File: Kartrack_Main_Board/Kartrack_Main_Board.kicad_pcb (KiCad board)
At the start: 4 copper layers, 130 x 80 mm, 69 parts, among them IC1 MIC3172YM, J2 Conn_Coaxial, J3 Conn_Coaxial, J4 Conn_01x02_Socket, J5 Conn_01x02_Socket, J6 USB_C_Receptacle_PowerOnly_6P, Q1 RE1C, SW1 SW_Push, SW2 SW_Push, SW3 SW_Push, U2 L76L-M33, U3 Ai-Thinker-Ra-02, U4 BQ21040DBV, U5 BU33SD5WG

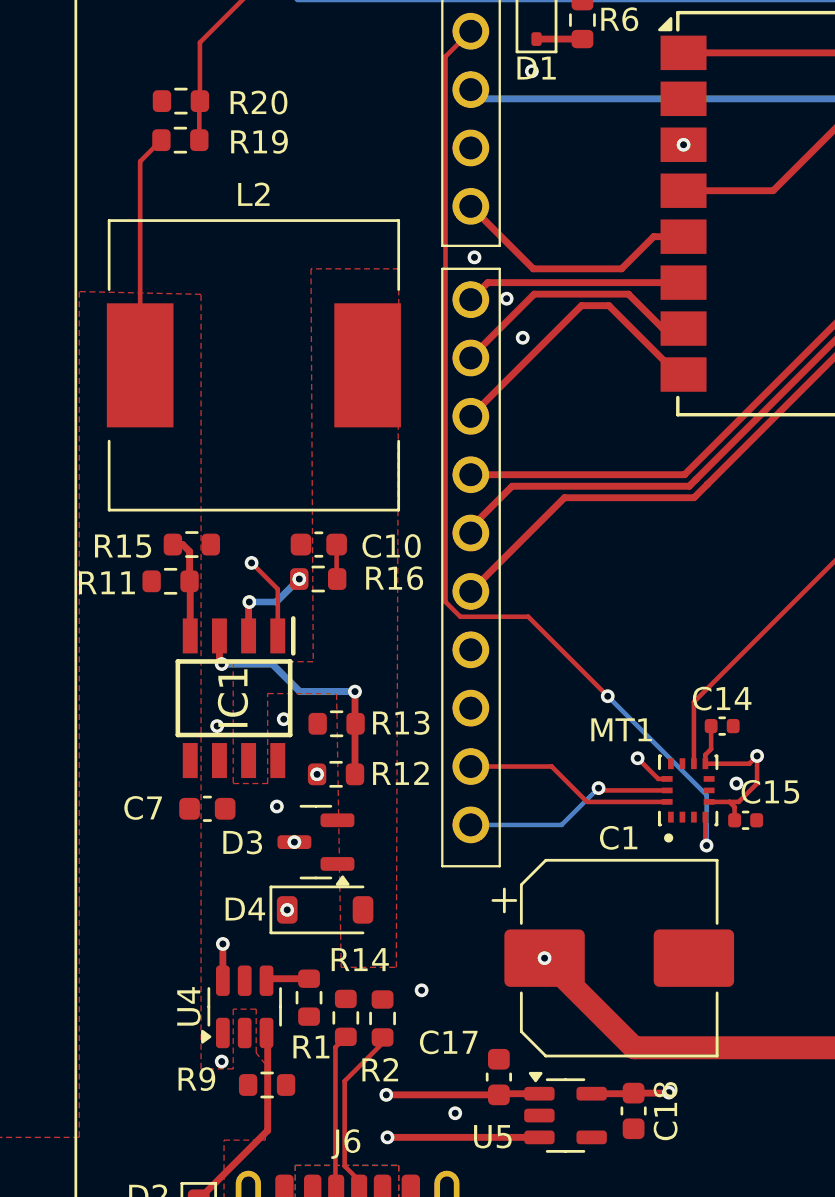
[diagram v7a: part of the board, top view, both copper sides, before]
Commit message: pcb via in pad remove
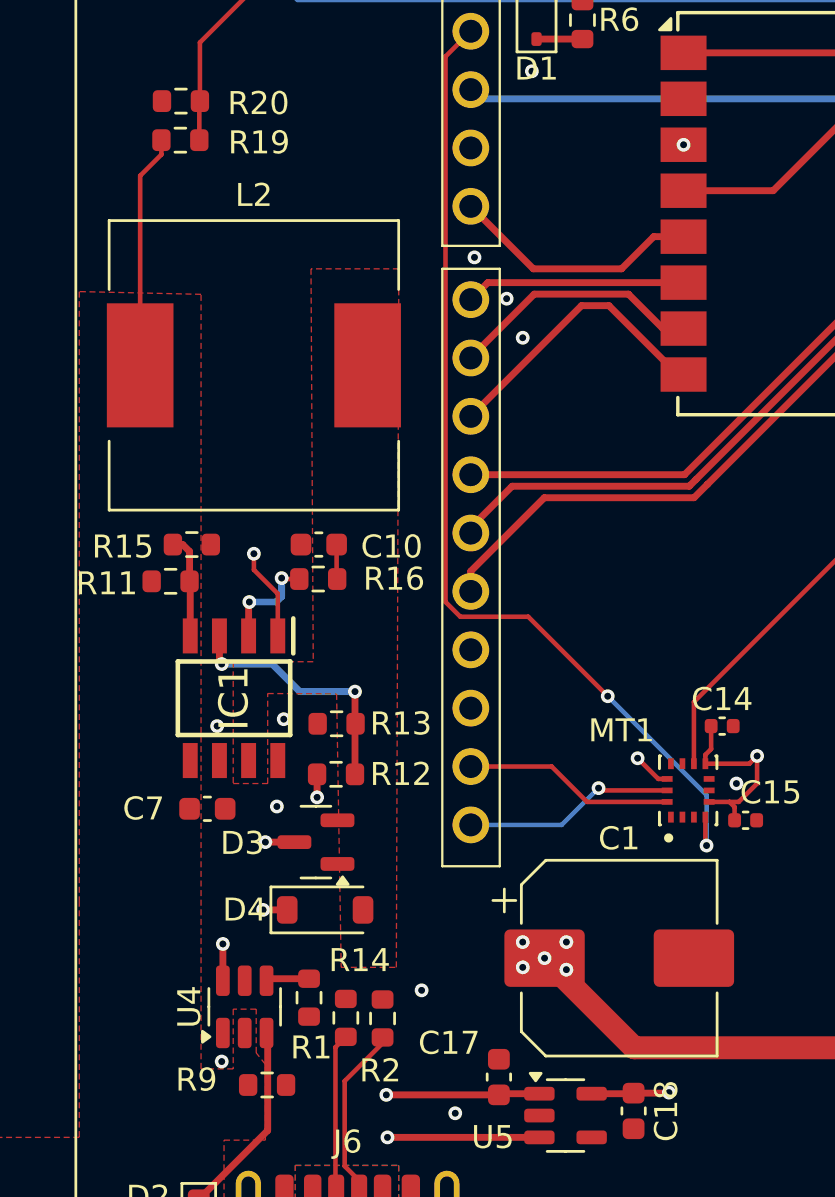
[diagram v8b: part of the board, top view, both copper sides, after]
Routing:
- net +5V: track 66.8 -> 70.1 mm, vias 13 -> 17
- net /CONN/PI1_SPI2_SCK: track 31.7 -> 32.2 mm
- net Net-(IC1-COMP): track 4.08 -> 4.59 mm
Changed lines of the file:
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@@
+	)
+	(segment
+		(start 153.55 115.5)
+		(end 153.55 116.5)
+		(width 0.3)
+		(layer "F.Cu")
+		(net 12)
 	)
 	(segment
@@
 	)
 	(segment
+		(start 152.25 121.4)
+		(end 151.2 121.4)
+		(width 0.3)
+		(layer "F.Cu")
+		(net 12)
+	)
+	(segment
+		(start 163.925 123.975)
+		(end 167.35 127.4)
+		(width 1)
+		(layer "F.Cu")
+		(net 12)
+	)
+	(segment
 		(start 149.45 122.8825)
 		(end 149.45 124.4825)
@@
 	(segment
 		(start 163.45 123.5)
-		(end 167.35 127.4)
+		(end 163.925 123.975)
 		(width 1)
 		(layer "F.Cu")
@@
 		(net 12)
 	)
+	(segment
+		(start 152.5625 118.45)
+		(end 151.3 118.45)
+		(width 0.3)
+		(layer "F.Cu")
+		(net 12)
+	)
 	(via
 		(at 163.45 123.5)
@@
 	)
 	(via
-		(at 153.55 115.5)
+		(at 153.55 116.5)
 		(size 0.6)
 		(drill 0.3)
@@
 	)
 	(via
+		(at 162.5 122.8)
+		(size 0.6)
+		(drill 0.3)
+		(layers "F.Cu" "B.Cu")
+		(net 12)
+	)
+	(via
+		(at 162.5 123.9)
+		(size 0.6)
+		(drill 0.3)
+		(layers "F.Cu" "B.Cu")
+		(net 12)
+	)
+	(via
 		(at 149.45 122.8825)
 		(size 0.6)
@@
 	)
 	(via
-		(at 152.5625 118.45)
-		(size 0.6)
-		(drill 0.3)
-		(layers "F.Cu" "B.Cu")
-		(net 12)
-	)
-	(via
-		(at 152.25 121.4)
+		(at 164.4 124)
+		(size 0.6)
+		(drill 0.3)
+		(layers "F.Cu" "B.Cu")
+		(net 12)
+	)
+	(via
+		(at 151.3 118.45)
+		(size 0.6)
+		(drill 0.3)
+		(layers "F.Cu" "B.Cu")
+		(net 12)
+	)
+	(via
+		(at 164.4 122.8)
+		(size 0.6)
+		(drill 0.3)
+		(layers "F.Cu" "B.Cu")
+		(net 12)
+	)
+	(via
+		(at 151.2 121.4)
 		(size 0.6)
 		(drill 0.3)
@@
 	)
 	(segment
-		(start 151.84 107.44)
-		(end 150.7 106.3)
-		(width 0.2)
-		(layer "F.Cu")
-		(net 17)
-	)
-	(segment
-		(start 151.84 109.476)
-		(end 151.84 107.44)
-		(width 0.2)
-		(layer "F.Cu")
-		(net 17)
-	)
-	(via
-		(at 150.7 106.3)
+		(start 150.8 106.6)
+		(end 151.84 107.64)
+		(width 0.2)
+		(layer "F.Cu")
+		(net 17)
+	)
+	(segment
+		(start 150.8 105.9)
+		(end 150.8 106.6)
+		(width 0.2)
+		(layer "F.Cu")
+		(net 17)
+	)
+	(segment
+		(start 151.84 107.64)
+		(end 151.84 109.476)
+		(width 0.2)
+		(layer "F.Cu")
+		(net 17)
+	)
+	(via
+		(at 150.8 105.9)
 		(size 0.6)
 		(drill 0.3)
@@
 	)
 	(segment
+		(start 163.438 103.462)
+		(end 160.24 106.66)
+		(width 0.3)
+		(layer "F.Cu")
+		(net 23)
+	)
+	(segment
+		(start 160.24 106.66)
+		(end 160.24 107.54)
+		(width 0.3)
+		(layer "F.Cu")
+		(net 23)
+	)
+	(segment
+		(start 185.5 92.1)
+		(end 181.31704 92.1)
+		(width 0.3)
+		(layer "F.Cu")
+		(net 23)
+	)
+	(segment
 		(start 181.31704 92.1)
 		(end 170.542 102.87504)
@@
 	)
 	(segment
-		(start 185.5 92.1)
-		(end 181.31704 92.1)
-		(width 0.3)
-		(layer "F.Cu")
-		(net 23)
-	)
-	(segment
 		(start 169.955042 103.462)
-		(end 164.318 103.462)
-		(width 0.3)
-		(layer "F.Cu")
-		(net 23)
-	)
-	(segment
-		(start 164.318 103.462)
-		(end 160.24 107.54)
+		(end 163.438 103.462)
 		(width 0.3)
 		(layer "F.Cu")
@@
 	)
 	(segment
-		(start 145.85 88.825)
+		(start 145.85 97.7)
+		(end 145.85 89.45)
+		(width 0.2)
+		(layer "F.Cu")
+		(net 30)
+	)
+	(segment
+		(start 146.775 88.525)
 		(end 146.775 87.9)
 		(width 0.2)
@@
 	)
 	(segment
-		(start 145.85 97.7)
-		(end 145.85 88.825)
+		(start 145.85 89.45)
+		(end 146.775 88.525)
 		(width 0.2)
 		(layer "F.Cu")
@@
 		(net 48)
 	)
+	(segment
+		(start 152.048529 107)
+		(end 152.007549 106.95902)
+		(width 0.2)
+		(layer "F.Cu")
+		(net 48)
+	)
+	(segment
+		(start 152.775 107)
+		(end 152.048529 107)
+		(width 0.2)
+		(layer "F.Cu")
+		(net 48)
+	)
 	(via
 		(at 150.6 108)
@@
 	)
 	(via
-		(at 152.775 107)
+		(at 152.007549 106.95902)
 		(size 0.6)
 		(drill 0.3)
@@
 	(segment
 		(start 151.775 108)
-		(end 152.775 107)
+		(end 150.6 108)
 		(width 0.3)
 		(layer "B.Cu")
@@
 	)
 	(segment
-		(start 150.6 108)
+		(start 152.007549 107.767451)
 		(end 151.775 108)
 		(width 0.3)
 		(layer "B.Cu")
+		(net 48)
+	)
+	(segment
+		(start 152.007549 106.95902)
+		(end 152.007549 107.767451)
+		(width 0.3)
+		(layer "B.Cu")
